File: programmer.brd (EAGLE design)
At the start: 44.9 x 15.7 mm, 14 parts, among them U1 FT232R, X1 53261-06

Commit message: Made mofications to schematics for readability
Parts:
- added FRAME1: (no value), SparkFun-Aesthetics:DUMMY
- added LOGO1: OSHW-LOGOS, SparkFun-Aesthetics:OSHW-LOGO-S
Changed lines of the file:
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@@
 <attribute name="VALUE" x="-2.54" y="11.168125" size="1.27" layer="27" rot="R270"/>
+</element>
+<element name="LOGO1" library="SparkFun-Aesthetics" package="OSHW-LOGO-S" value="OSHW-LOGOS" x="4.60375" y="13.6525"/>
+<element name="FRAME1" library="SparkFun-Aesthetics" package="DUMMY" value="" x="-0.79375" y="-1.11125">
+<attribute name="VERSION" value="v01" x="-0.79375" y="-1.11125" size="1.778" layer="27" display="off"/>
+<attribute name="DESIGNER" value="Nobody" x="-0.79375" y="-1.11125" size="1.778" layer="27" display="off"/>
 </element>
 </elements>
@@
 <via x="25.4" y="11.1125" extent="1-16" drill="0.6"/>
 <wire x1="22.31625" y1="9.6885" x2="22.31625" y2="10.63625" width="0.254" layer="1"/>
-<via x="10.63625" y="6.0325" extent="1-16" drill="0.6"/>
+<via x="9.2075" y="1.74625" extent="1-16" drill="0.6"/>
 <via x="25.7175" y="3.96875" extent="1-16" drill="0.6"/>
 </signal>

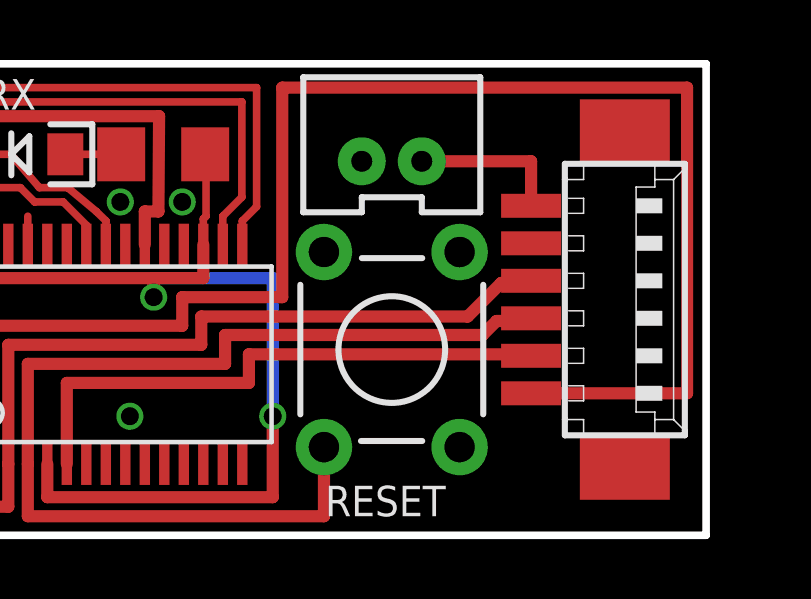
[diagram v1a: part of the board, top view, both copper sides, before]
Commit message: Revision of programmer board to include a SMD 6 pin FTDI header.
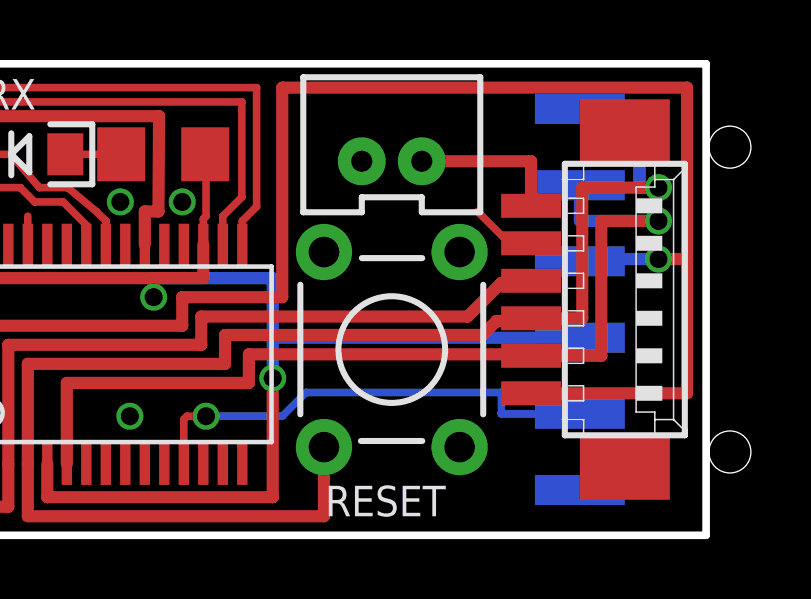
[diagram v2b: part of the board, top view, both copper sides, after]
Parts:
- added JP2: RA 6Pin SMD, SparkFun-Connectors:1X06-SMD
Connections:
- net 3.3V: now also JP2.4
- net CTS: now also JP2.5
- net GND: now also JP2.6
- net RTS: now also JP2.1
- net RXD: now also JP2.2
- net TXD: now also JP2.3
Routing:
- net CTS: track 0.00 -> 15.8 mm, vias 0 -> 1
- net RTS: track 35.2 -> 50.3 mm, vias 0 -> 1
- net RXD: track 19.2 -> 31.7 mm, vias 0 -> 1
- net 3.3V: track 50.3 -> 60.5 mm
- net TXD: track 51.2 -> 56.1 mm, vias 0 -> 1
- net GND: track 0.95 -> 3.17 mm
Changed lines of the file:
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@@
 <attribute name="DESIGNER" value="Nobody" x="-0.79375" y="-1.11125" size="1.778" layer="27" display="off"/>
+</element>
+<element name="JP2" library="SparkFun-Connectors" package="1X06-SMD" value="RA 6Pin SMD" x="45.72" y="7.858125" rot="MR270">
+<attribute name="PROD_ID" value="CONN-08971" x="45.72" y="7.858125" size="1.778" layer="28" rot="MR270" display="off"/>
 </element>
 </elements>
@@
 <via x="9.2075" y="1.74625" extent="1-16" drill="0.6"/>
 <via x="25.7175" y="3.96875" extent="1-16" drill="0.6"/>
+<contactref element="JP2" pad="6"/>
+<wire x1="39.0925" y1="9.733125" x2="38.368125" y2="9.733125" width="0.254" layer="1"/>
+<wire x1="38.368125" y1="9.733125" x2="37.30625" y2="10.795" width="0.254" layer="1"/>
 </signal>
 <signal name="12V">
@@
 <wire x1="22.96625" y1="2.3765" x2="22.96625" y2="1.27" width="0.4064" layer="1"/>
 <wire x1="22.96625" y1="1.27" x2="30.48" y2="1.27" width="0.4064" layer="1"/>
-<wire x1="30.48" y1="1.27" x2="30.48" y2="3.96875" width="0.4064" layer="1"/>
-<via x="30.48" y="3.96875" extent="1-16" drill="0.6"/>
-<wire x1="30.48" y1="3.96875" x2="30.48" y2="8.5725" width="0.4064" layer="16"/>
+<wire x1="30.48" y1="1.27" x2="30.48" y2="5.23875" width="0.4064" layer="1"/>
+<via x="30.48" y="5.23875" extent="1-16" drill="0.6"/>
+<wire x1="30.48" y1="5.23875" x2="30.48" y2="6.50875" width="0.4064" layer="16"/>
+<wire x1="30.48" y1="6.588125" x2="30.48" y2="8.5725" width="0.4064" layer="16"/>
 <wire x1="30.48" y1="8.5725" x2="26.51125" y2="8.5725" width="0.4064" layer="16"/>
 <wire x1="26.51125" y1="8.5725" x2="26.51125" y2="7.9375" width="0.4064" layer="16"/>
@@
 <wire x1="17.4625" y1="10.00125" x2="18.57375" y2="10.00125" width="0.254" layer="1"/>
 <wire x1="18.57375" y1="10.00125" x2="18.57375" y2="10.44875" width="0.254" layer="1"/>
+<contactref element="JP2" pad="4"/>
+<wire x1="40.72" y1="6.588125" x2="30.48" y2="6.588125" width="0.4064" layer="16"/>
+<wire x1="30.48" y1="6.588125" x2="30.48" y2="6.50875" width="0.4064" layer="16"/>
 </signal>
 <signal name="VCC" class="1">
@@
 <wire x1="30.7975" y1="7.9375" x2="30.7975" y2="14.9225" width="0.4064" layer="1"/>
 <wire x1="30.7975" y1="14.9225" x2="44.29125" y2="14.9225" width="0.4064" layer="1"/>
-<wire x1="44.29125" y1="14.9225" x2="44.29125" y2="4.733125" width="0.4064" layer="1"/>
+<wire x1="44.29125" y1="14.9225" x2="44.29125" y2="9.2075" width="0.4064" layer="1"/>
+<contactref element="JP2" pad="3"/>
 <wire x1="39.0925" y1="4.733125" x2="44.29125" y2="4.733125" width="0.4064" layer="1"/>
+<wire x1="44.29125" y1="4.733125" x2="44.29125" y2="9.2075" width="0.4064" layer="1"/>
+<wire x1="44.29125" y1="9.2075" x2="43.33875" y2="9.2075" width="0.4064" layer="1"/>
+<via x="43.33875" y="9.2075" extent="1-16" drill="0.6"/>
+<wire x1="43.33875" y1="9.2075" x2="40.085" y2="9.2075" width="0.4064" layer="16"/>
+<wire x1="40.085" y1="9.2075" x2="40.72" y2="9.128125" width="0.4064" layer="16"/>
 </signal>
 <signal name="RXD">
@@
 <wire x1="23.61625" y1="5.08" x2="23.61625" y2="2.3765" width="0.4064" layer="1"/>
 <wire x1="39.043125" y1="6.0325" x2="39.0925" y2="5.983125" width="0.4064" layer="1"/>
+<contactref element="JP2" pad="2"/>
+<wire x1="40.72" y1="11.668125" x2="40.72" y2="10.4775" width="0.4064" layer="16"/>
+<wire x1="40.72" y1="10.4775" x2="43.33875" y2="10.4775" width="0.4064" layer="16"/>
+<via x="43.33875" y="10.4775" extent="1-16" drill="0.6"/>
+<wire x1="43.33875" y1="10.4775" x2="41.43375" y2="10.4775" width="0.4064" layer="1"/>
+<wire x1="41.43375" y1="10.4775" x2="41.43375" y2="5.983125" width="0.4064" layer="1"/>
+<wire x1="39.0925" y1="5.983125" x2="41.43375" y2="5.983125" width="0.4064" layer="1"/>
 </signal>
 <signal name="RTS">
@@
 <wire x1="37.94125" y1="7.14375" x2="39.003125" y2="7.14375" width="0.4064" layer="1"/>
 <wire x1="39.003125" y1="7.14375" x2="39.0925" y2="7.233125" width="0.4064" layer="1"/>
+<contactref element="JP2" pad="1"/>
+<wire x1="39.0925" y1="7.233125" x2="40.79875" y2="7.233125" width="0.4064" layer="1"/>
+<wire x1="40.79875" y1="7.233125" x2="40.79875" y2="11.58875" width="0.4064" layer="1"/>
+<wire x1="40.79875" y1="11.58875" x2="43.33875" y2="11.58875" width="0.4064" layer="1"/>
+<via x="43.33875" y="11.58875" extent="1-16" drill="0.6"/>
+<wire x1="43.33875" y1="11.58875" x2="42.70375" y2="11.58875" width="0.4064" layer="16"/>
+<wire x1="42.70375" y1="11.58875" x2="42.70375" y2="14.12875" width="0.4064" layer="16"/>
+<wire x1="42.70375" y1="14.12875" x2="40.085" y2="14.12875" width="0.4064" layer="16"/>
+<wire x1="40.085" y1="14.12875" x2="40.72" y2="14.208125" width="0.4064" layer="16"/>
 </signal>
 <signal name="CTS">
 <contactref element="U1" pad="11"/>
+<contactref element="JP2" pad="5"/>
+<wire x1="40.72" y1="4.048125" x2="38.1" y2="4.048125" width="0.254" layer="16"/>
+<wire x1="38.1" y1="4.048125" x2="38.1" y2="4.7625" width="0.254" layer="16"/>
+<wire x1="38.1" y1="4.7625" x2="31.59125" y2="4.7625" width="0.254" layer="16"/>
+<wire x1="31.59125" y1="4.7625" x2="30.7975" y2="3.96875" width="0.254" layer="16"/>
+<wire x1="30.7975" y1="3.96875" x2="28.2575" y2="3.96875" width="0.254" layer="16"/>
+<via x="28.2575" y="3.96875" extent="1-16" drill="0.6"/>
+<wire x1="28.2575" y1="3.96875" x2="27.6225" y2="3.96875" width="0.254" layer="1"/>
+<wire x1="27.51625" y1="2.3765" x2="27.51625" y2="3.8625" width="0.254" layer="1"/>
+<wire x1="27.51625" y1="3.8625" x2="27.6225" y2="3.96875" width="0.254" layer="1"/>
 </signal>
 <signal name="DTR">

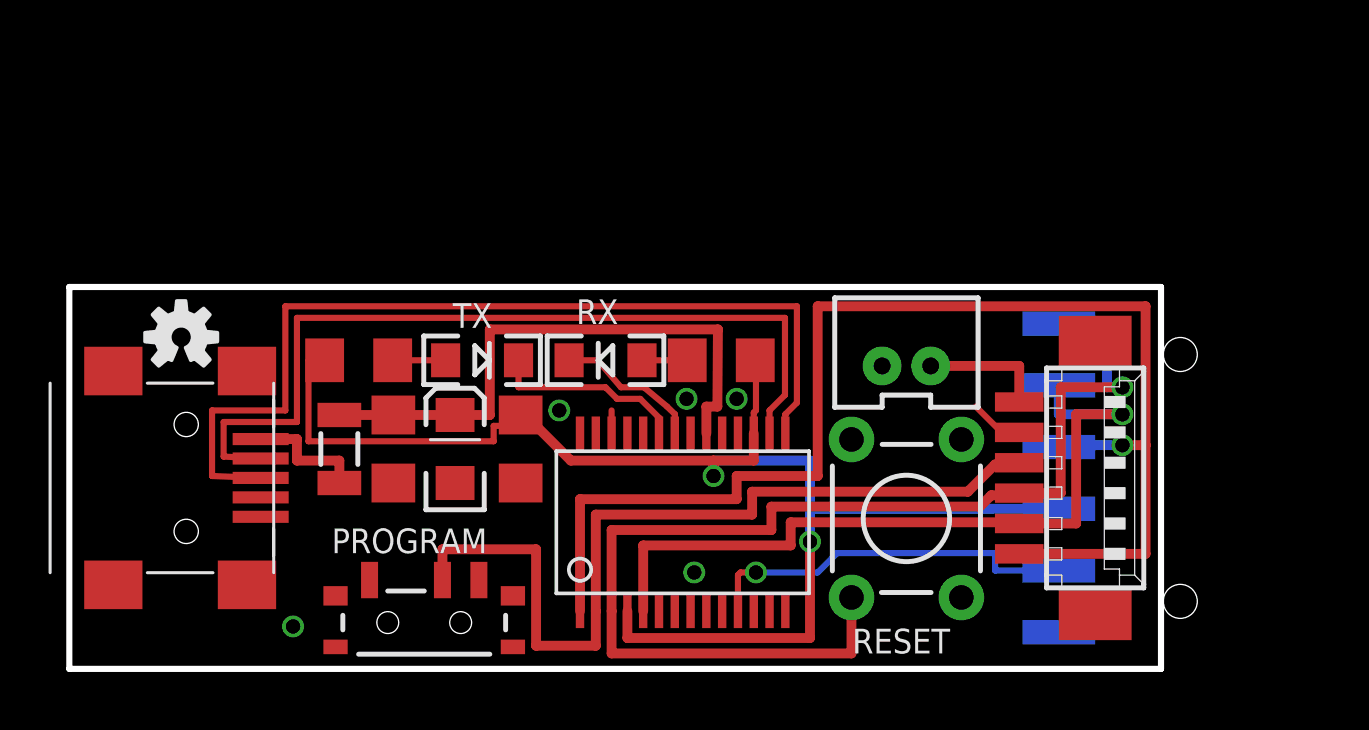
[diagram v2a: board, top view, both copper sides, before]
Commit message: Changed to CH340G + Crystal instead of FT232RL Resolves #4. Using 12 Volt Barrel Jack Resolves #3. Moved to Omron 10xxx switches instead of slider, Resolves #1
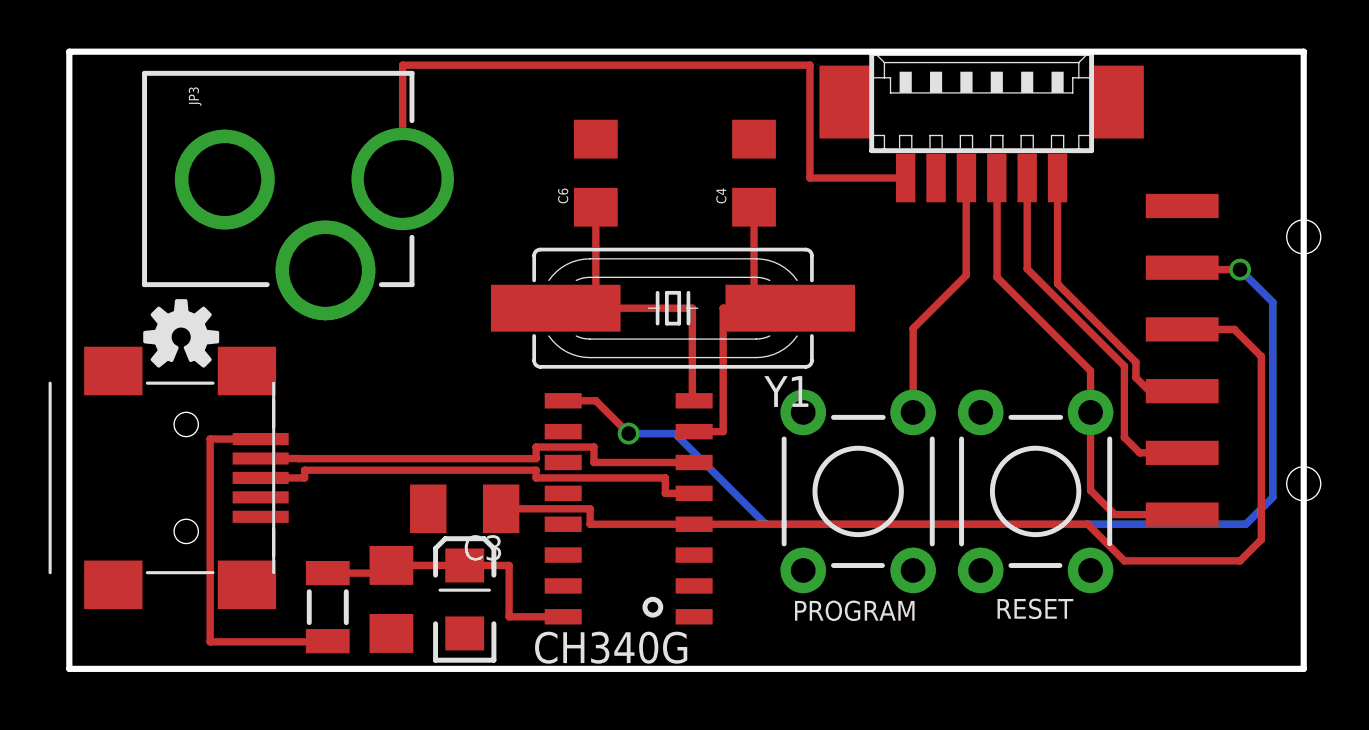
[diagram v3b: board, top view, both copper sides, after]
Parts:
- removed C1: 0.1uF, SparkFun-Passives:1206
- removed JP1: 12V DC, SparkFun-Connectors:JST-2-PTH-VERT
- removed R1, R2: 330, SparkFun-Passives:1206
- removed RX: GREEN, SparkFun-LED:LED-1206
- removed TX: RED, SparkFun-LED:LED-1206
- removed U1: FT232R, SparkFun:SSOP28DB
- added C3: 0.1uF, rcl:C1206K
- added C4, C6: 22pf, SparkFun-Capacitors:1206
- added JP3: POWER_JACKPTH_LOCK, SparkFun-Connectors:POWER_JACK_PTH_LOCK
- added U$1: CH340G, CH340G-USB-SERIAL:SOIC16
- added Y1: 12mhz, SparkFun-FreqCtrl:HC49UP
- PROGRAM: value (none) -> SWITCH-MOMENTARY-2PTH; device SparkFun-Electromechanical:SWITCH-SPST-SMD-A -> SparkFun-Electromechanical:TACTILE-PTH
- moved PROGRAM 18.7 mm to (32.5, 7.30), turned to 270 degrees
- moved X1 15.4 mm to (37.5, 22.7), turned to 0 degrees
- moved JP2 7.02 mm to (50.8, 12.7), flipped to the top, turned to 90 degrees
- moved F1 6.53 mm to (10.6, 2.54)
- moved C5 6.20 mm to (16.3, 2.86)
- moved C2 6.19 mm to (13.3, 2.86)
- moved RESET 5.43 mm to (39.8, 7.30), turned to 270 degrees
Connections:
- removed net DCD: U1.10
- removed net DSR: U1.9
- removed net DTR: PROGRAM.2, U1.2, X1.4
- removed net N$1: R1.1, TX.A
- removed net N$2: R2.1, RX.A
- removed net PWREN: U1.14
- removed net RI: U1.6
- removed net RTS: JP2.1, RESET.1, U1.3, X1.3
- removed net RXLED: RX.C, U1.22
- removed net SLEEP: U1.12
- removed net TXDEN: U1.13
- removed net TXLED: TX.C, U1.23
- new net GPIO0: PROGRAM.1, X1.4
- new net OSCI: C4.1, U$1.7, Y1.1
- new net OSCO: C6.1, U$1.8, Y1.2
- new net RESET: JP2.1, RESET.1, X1.3
- new net RX: U$1.2
- new net TX: U$1.3
- net 12V: now also JP3.PWR; no longer JP1.2
- net 3.3V: now also C3.1, U$1.4; no longer C1.1, R1.2, R2.2, U1.17, U1.4
- net CTS: now also U$1.9; no longer U1.11
- net GND: now also C3.2, C4.2, C6.2, JP3.GND, JP3.GNDBREAK, U$1.1; no longer C1.2, JP1.1, U1.18, U1.21, U1.25, U1.26, U1.7
- net RXD: no longer U1.5
- net TXD: no longer U1.1
- net USB_D+: now also U$1.5; no longer U1.15
- net USB_D-: now also U$1.6; no longer U1.16
- net VCC: now also U$1.16; no longer U1.20
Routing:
- net RTS: track 50.3 -> 0.00 mm, vias 1 -> 0
- net TXD: track 56.1 -> 11.7 mm, vias 1 -> 0
- net DTR: track 35.8 -> 0.00 mm
- net CTS: track 15.8 -> 44.1 mm, vias 1 -> 2
- net 12V: track 5.13 -> 30.0 mm
- net USB_D+: track 38.5 -> 19.1 mm
- net RESET: track 0.00 -> 18.6 mm
- net RXD: track 31.7 -> 15.0 mm, vias 1 -> 0
- net USB_D-: track 35.4 -> 19.0 mm
- net 3.3V: track 60.5 -> 44.2 mm, vias 2 -> 0
- net OSCO: track 0.00 -> 13.7 mm
- net OSCI: track 0.00 -> 13.2 mm
- net VCC: track 23.8 -> 12.1 mm
- net GPIO0: track 0.00 -> 10.6 mm
- net N$3: track 5.05 -> 15.3 mm
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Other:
- board size 44.9 x 15.7 mm -> 50.8 x 25.4 mm
